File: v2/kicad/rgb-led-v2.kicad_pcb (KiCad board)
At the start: 2 copper layers, 90 x 50 mm, 12 parts, among them SW1 SPST

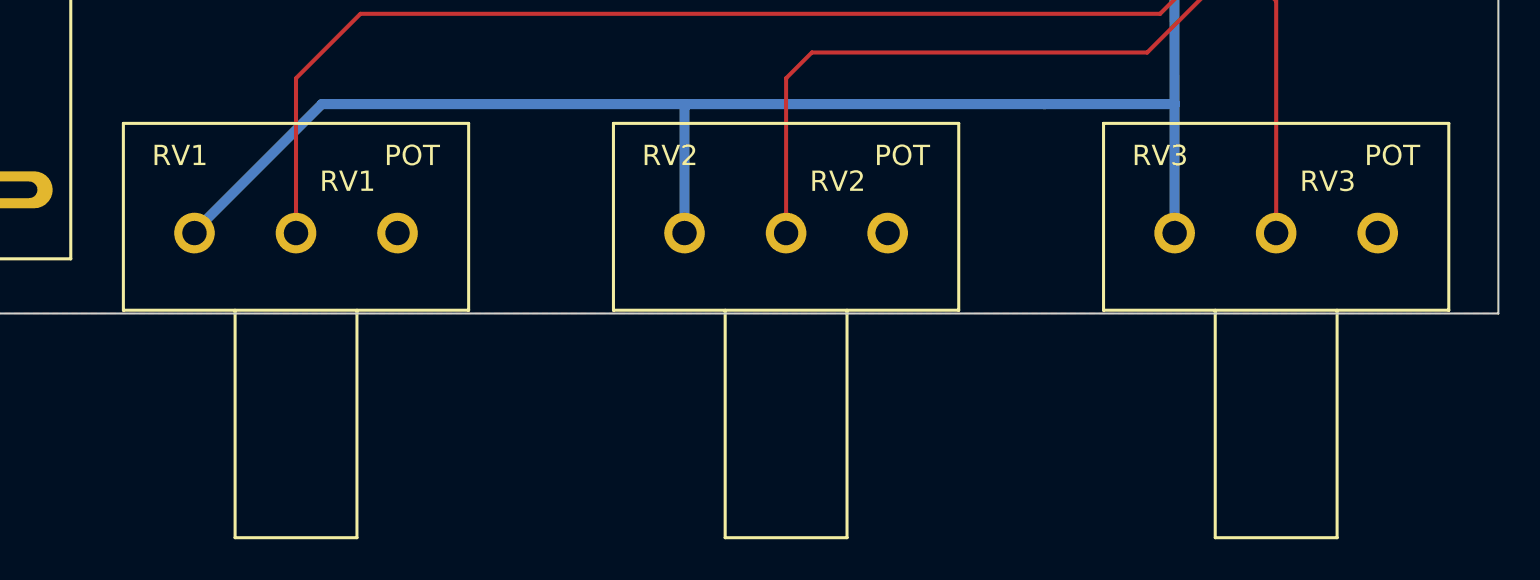
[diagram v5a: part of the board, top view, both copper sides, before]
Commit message: [v2] Removed outline of pot
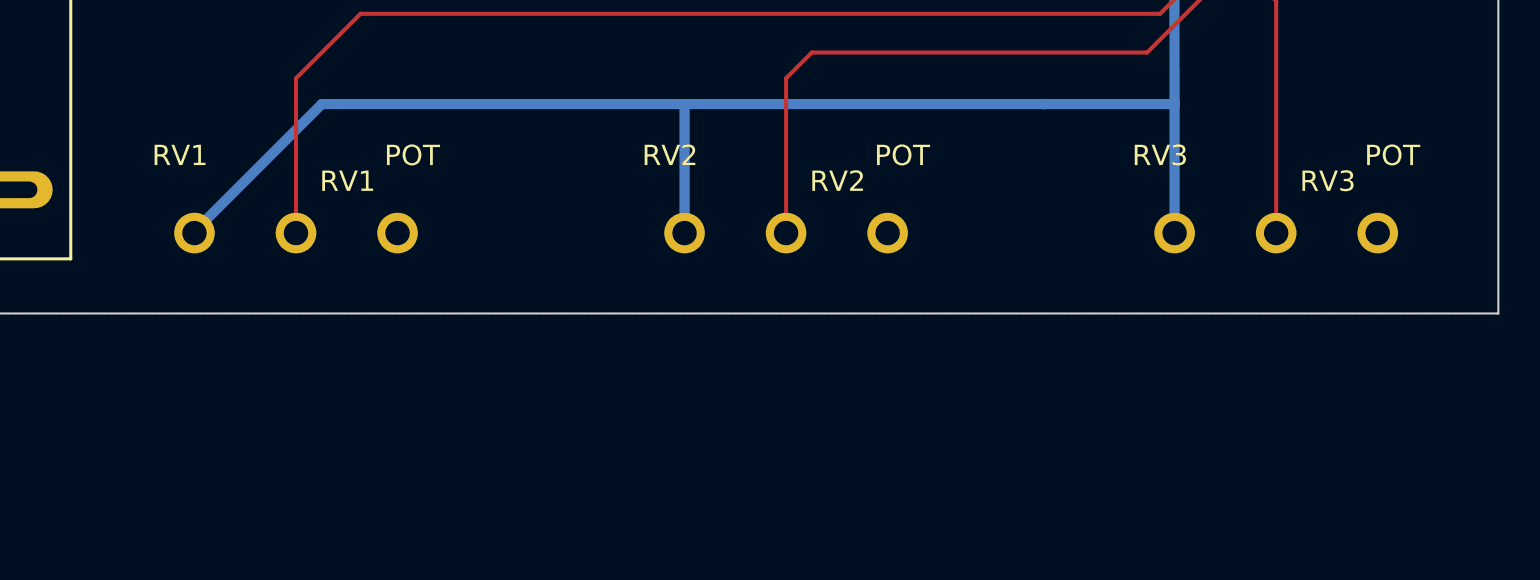
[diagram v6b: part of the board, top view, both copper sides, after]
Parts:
- RV2, RV3: footprint POT_3 -> POT_3_Naked
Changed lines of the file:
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@@
     (links 26)
     (no_connects 0)
-    (area 18.679999 19.949999 118.544049 81.130001)
+    (area 18.679999 19.949999 118.544049 70.050001)
     (thickness 1.6)
     (drawings 35)
@@
   )
   (setup
-    (last_trace_width 1.38)
+    (last_trace_width 0.01)
     (user_trace_width 0.2)
     (user_trace_width 0.5)
@@
     (pad_to_mask_clearance 0)
     (aux_axis_origin 0 0)
-    (visible_elements FFFE0909)
+    (visible_elements FFFE2909)
     (pcbplotparams
-      (layerselection 3178497)
+      (layerselection 2097152)
       (usegerberextensions true)
       (excludeedgelayer true)
@@
       (psnegative false)
       (psa4output false)
-      (plotreference true)
-      (plotvalue true)
-      (plotothertext true)
+      (plotreference false)
+      (plotvalue false)
+      (plotothertext false)
       (plotinvisibletext false)
       (padsonsilk false)
@@
       (drillshape 0)
       (scaleselection 1)
-      (outputdirectory ""))
+      (outputdirectory gerber/))
   )
   (net 0 "")
@@
       (effects (font (size 1 1) (thickness 0.15)))
     )
-    (fp_line (start -3 3.8) (end -3 15) (layer F.SilkS) (width 0.15))
-    (fp_line (start -3 15) (end 3 15) (layer F.SilkS) (width 0.15))
-    (fp_line (start 3 15) (end 3 3.8) (layer F.SilkS) (width 0.15))
-    (fp_line (start -8.5 3.8) (end 8.5 3.8) (layer F.SilkS) (width 0.15))
-    (fp_line (start -8.5 -5.4) (end 8.5 -5.4) (layer F.SilkS) (width 0.15))
-    (fp_line (start -8.5 -5.4) (end -8.5 3.8) (layer F.SilkS) (width 0.15))
-    (fp_line (start 8.5 -5.4) (end 8.5 3.8) (layer F.SilkS) (width 0.15))
     (pad 1 thru_hole circle (at -5 0) (size 2 2) (drill 1.2)
       (layers *.Cu *.Mask F.SilkS)
@@
       (layers *.Cu *.Mask F.SilkS)
       (net 9 N-000003)
-    )
-    (pad 3 thru_hole circle (at 5 0) (size 2 2) (drill 1.2)
-      (layers *.Cu *.Mask F.SilkS)
-      (net 1 GND)
-    )
-  )
-  (module POT_3 (layer F.Cu)
-    (at 73.66 66.04)
-    (fp_text reference RV2 (at -5.715 -3.81) (layer F.SilkS)
-      (effects (font (size 1 1) (thickness 0.15)))
-    )
-    (fp_text value POT (at 5.715 -3.81) (layer F.SilkS)
-      (effects (font (size 1 1) (thickness 0.15)))
-    )
-    (fp_line (start -3 3.8) (end -3 15) (layer F.SilkS) (width 0.15))
-    (fp_line (start -3 15) (end 3 15) (layer F.SilkS) (width 0.15))
-    (fp_line (start 3 15) (end 3 3.8) (layer F.SilkS) (width 0.15))
-    (fp_line (start -8.5 3.8) (end 8.5 3.8) (layer F.SilkS) (width 0.15))
-    (fp_line (start -8.5 -5.4) (end 8.5 -5.4) (layer F.SilkS) (width 0.15))
-    (fp_line (start -8.5 -5.4) (end -8.5 3.8) (layer F.SilkS) (width 0.15))
-    (fp_line (start 8.5 -5.4) (end 8.5 3.8) (layer F.SilkS) (width 0.15))
-    (pad 1 thru_hole circle (at -5 0) (size 2 2) (drill 1.2)
-      (layers *.Cu *.Mask F.SilkS)
-      (net 2 N-000001)
-    )
-    (pad 2 thru_hole circle (at 0 0) (size 2 2) (drill 1.2)
-      (layers *.Cu *.Mask F.SilkS)
-      (net 10 N-000004)
-    )
-    (pad 3 thru_hole circle (at 5 0) (size 2 2) (drill 1.2)
-      (layers *.Cu *.Mask F.SilkS)
-      (net 1 GND)
-    )
-  )
-  (module POT_3 (layer F.Cu)
-    (at 97.79 66.04)
-    (fp_text reference RV3 (at -5.715 -3.81) (layer F.SilkS)
-      (effects (font (size 1 1) (thickness 0.15)))
-    )
-    (fp_text value POT (at 5.715 -3.81) (layer F.SilkS)
-      (effects (font (size 1 1) (thickness 0.15)))
-    )
-    (fp_line (start -3 3.8) (end -3 15) (layer F.SilkS) (width 0.15))
-    (fp_line (start -3 15) (end 3 15) (layer F.SilkS) (width 0.15))
-    (fp_line (start 3 15) (end 3 3.8) (layer F.SilkS) (width 0.15))
-    (fp_line (start -8.5 3.8) (end 8.5 3.8) (layer F.SilkS) (width 0.15))
-    (fp_line (start -8.5 -5.4) (end 8.5 -5.4) (layer F.SilkS) (width 0.15))
-    (fp_line (start -8.5 -5.4) (end -8.5 3.8) (layer F.SilkS) (width 0.15))
-    (fp_line (start 8.5 -5.4) (end 8.5 3.8) (layer F.SilkS) (width 0.15))
-    (pad 1 thru_hole circle (at -5 0) (size 2 2) (drill 1.2)
-      (layers *.Cu *.Mask F.SilkS)
-      (net 2 N-000001)
-    )
-    (pad 2 thru_hole circle (at 0 0) (size 2 2) (drill 1.2)
-      (layers *.Cu *.Mask F.SilkS)
-      (net 11 N-000005)
     )
     (pad 3 thru_hole circle (at 5 0) (size 2 2) (drill 1.2)
@@
     )
   )
+  (module POT_3_Naked (layer F.Cu)
+    (at 73.66 66.04)
+    (fp_text reference RV2 (at -5.715 -3.81) (layer F.SilkS)
+      (effects (font (size 1 1) (thickness 0.15)))
+    )
+    (fp_text value POT (at 5.715 -3.81) (layer F.SilkS)
+      (effects (font (size 1 1) (thickness 0.15)))
+    )
+    (pad 1 thru_hole circle (at -5 0) (size 2 2) (drill 1.2)
+      (layers *.Cu *.Mask F.SilkS)
+      (net 2 N-000001)
+    )
+    (pad 2 thru_hole circle (at 0 0) (size 2 2) (drill 1.2)
+      (layers *.Cu *.Mask F.SilkS)
+      (net 10 N-000004)
+    )
+    (pad 3 thru_hole circle (at 5 0) (size 2 2) (drill 1.2)
+      (layers *.Cu *.Mask F.SilkS)
+      (net 1 GND)
+    )
+  )
+  (module POT_3_Naked (layer F.Cu)
+    (at 97.79 66.04)
+    (fp_text reference RV3 (at -5.715 -3.81) (layer F.SilkS)
+      (effects (font (size 1 1) (thickness 0.15)))
+    )
+    (fp_text value POT (at 5.715 -3.81) (layer F.SilkS)
+      (effects (font (size 1 1) (thickness 0.15)))
+    )
+    (pad 1 thru_hole circle (at -5 0) (size 2 2) (drill 1.2)
+      (layers *.Cu *.Mask F.SilkS)
+      (net 2 N-000001)
+    )
+    (pad 2 thru_hole circle (at 0 0) (size 2 2) (drill 1.2)
+      (layers *.Cu *.Mask F.SilkS)
+      (net 11 N-000005)
+    )
+    (pad 3 thru_hole circle (at 5 0) (size 2 2) (drill 1.2)
+      (layers *.Cu *.Mask F.SilkS)
+      (net 1 GND)
+    )
+  )
